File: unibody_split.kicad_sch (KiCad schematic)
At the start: 91 parts

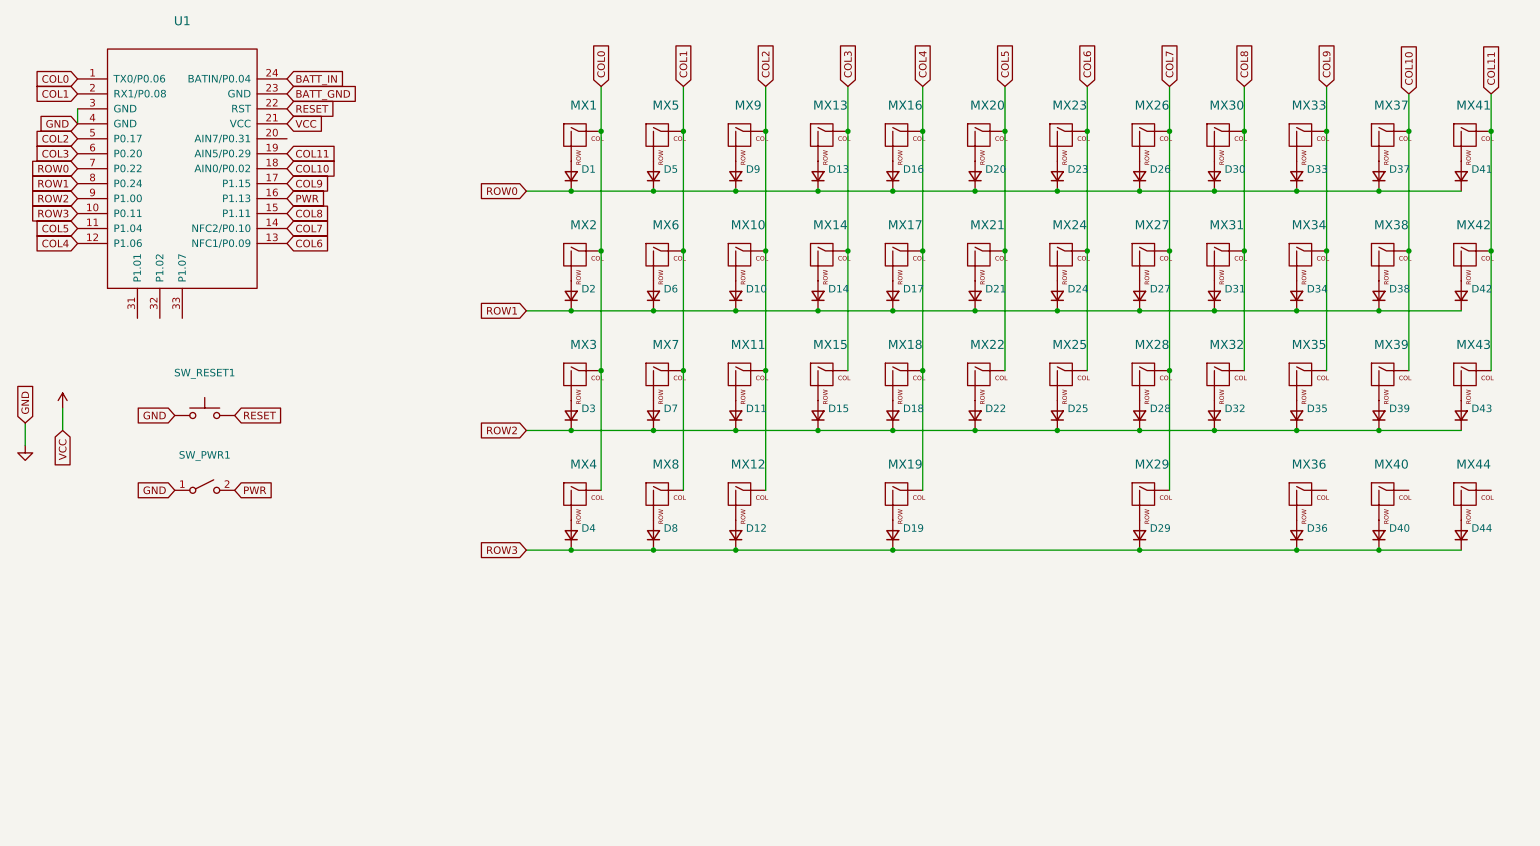
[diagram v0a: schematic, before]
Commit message: Adds kbd library, wires everything up
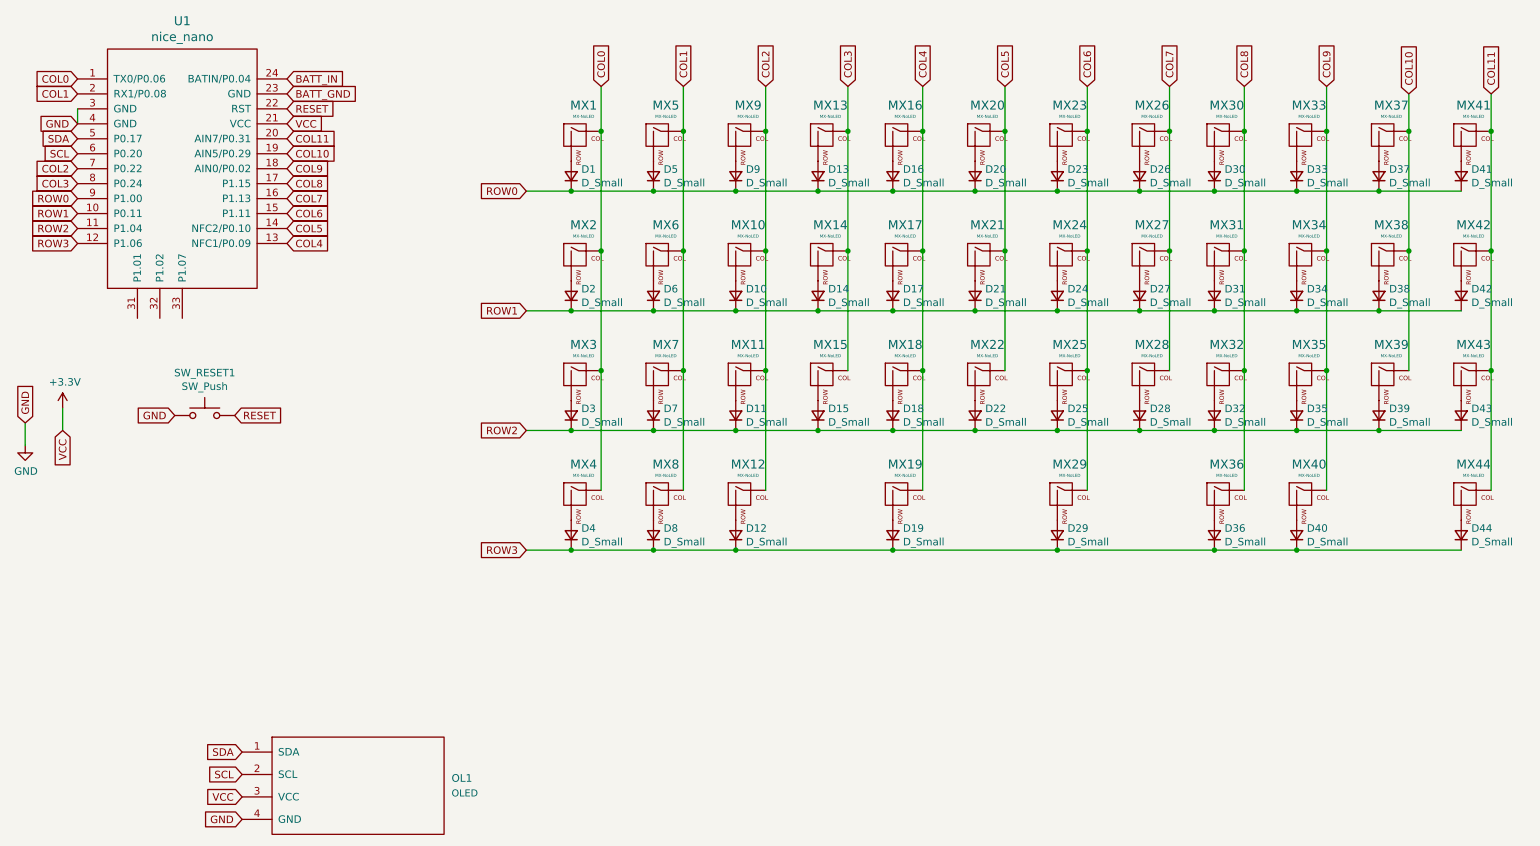
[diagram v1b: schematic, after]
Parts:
- removed SW_PWR1: (no value), symbol Switch:SW_SPST
- added OL1: OLED, kbd:OLED_v2, symbol kbd:OLED
- D1, D10, D11, D12, D13, D14, D15, D16, D17, D18, D19, D2, D20, D21, D22, D23, D24, D25, D26, D27, D28, D29, D3, D30, D31, D32, D33, D34, D35, D36, D37, D38, D39, D4, D40, D41, D42, D43, D44, D5, D6, D7, D8, D9: value (none) -> D_Small; footprint (none) -> Diode_SMD:D_SOD-123
- MX1, MX10, MX11, MX13, MX14, MX15, MX16, MX17, MX18, MX20, MX21, MX22, MX23, MX24, MX25, MX26, MX27, MX28, MX30, MX31, MX32, MX33, MX34, MX35, MX37, MX38, MX39, MX43, MX5, MX6, MX7, MX9: value (none) -> MX-NoLED; footprint (none) -> MX_Only:MXOnly-1U-Hotswap
- MX12, MX19, MX2, MX29, MX3, MX36, MX4, MX40, MX41, MX42, MX44, MX8: value (none) -> MX-NoLED
- SW_RESET1: value (none) -> SW_Push; footprint (none) -> random-keyboard-parts:SKQG-1155865
- U1: value (none) -> nice_nano; footprint (none) -> nice-nano-kicad:nice_nano
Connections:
- net PWR is gone; now on net COL7: U1.16 (P1.13)
- net +3V3: now also OL1.3 (VCC)
- net COL10: now also U1.19 (AIN5/P0.29); no longer U1.18 (AIN0/P0.02)
- net COL11: now also MX44.1 (COL), U1.20 (AIN7/P0.31); no longer U1.19 (AIN5/P0.29)
- net COL2: now also U1.7 (P0.22); no longer U1.5 (P0.17)
- net COL3: now also U1.8 (P0.24); no longer U1.6 (P0.20)
- net COL4: now also U1.13 (NFC1/P0.09); no longer U1.12 (P1.06)
- net COL5: now also U1.14 (NFC2/P0.10); no longer U1.11 (P1.04)
- net COL6: now also MX29.1 (COL), U1.15 (P1.11); no longer U1.13 (NFC1/P0.09)
- net COL7: no longer MX29.1 (COL), U1.14 (NFC2/P0.10)
- net COL8: now also MX36.1 (COL), U1.17 (P1.15); no longer U1.15 (P1.11)
- net COL9: now also MX40.1 (COL), U1.18 (AIN0/P0.02); no longer U1.17 (P1.15)
- net GND: now also OL1.4 (GND)
- net ROW0: now also U1.9 (P1.00); no longer U1.7 (P0.22)
- net ROW1: now also U1.10 (P0.11); no longer U1.8 (P0.24)
- net ROW2: now also U1.11 (P1.04); no longer U1.9 (P1.00)
- net ROW3: now also U1.12 (P1.06); no longer U1.10 (P0.11)
- new net SCL: OL1.2 (SCL), U1.6 (P0.20)
- new net SDA: OL1.1 (SDA), U1.5 (P0.17)
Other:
- moved on the sheet: D29, D36, D40, MX29, MX36, MX40

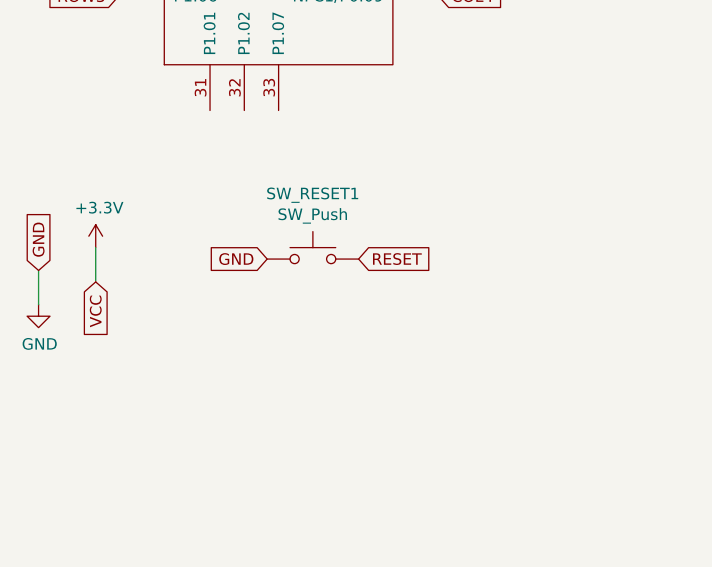
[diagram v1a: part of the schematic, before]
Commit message: Adds smaller reset switch, JST for battery
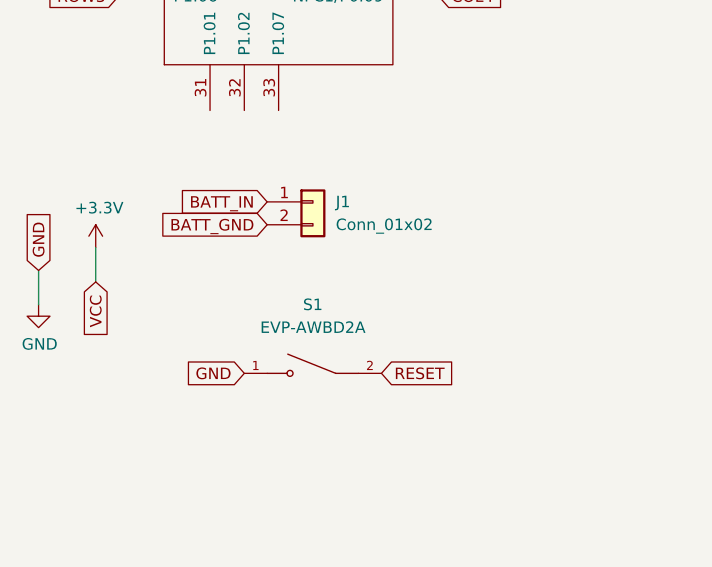
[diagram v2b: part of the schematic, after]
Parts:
- removed SW_RESET1: SW_Push, random-keyboard-parts:SKQG-1155865, symbol Switch:SW_Push
- added J1: Conn_01x02, Connector_JST:JST_PH_S2B-PH-SM4-TB_1x02-1MP_P2.00mm_Horizontal, symbol Connector_Generic:Conn_01x02
- added S1: EVP-AWBD2A, switches:SW_EVP-AWBD2A, symbol EVP-AWBD2A:EVP-AWBD2A
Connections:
- net BATT_GND: now also J1.2 (Pin_2)
- net BATT_IN: now also J1.1 (Pin_1)
- net GND: now also S1.1
- net RESET: now also S1.2
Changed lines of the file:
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@@
     )
   )
-  (global_label "GND" (shape input) (at 43.18 87.63 180) (fields_autoplaced)
+  (global_label "GND" (shape input) (at 40.64 100.33 180) (fields_autoplaced)
     (effects (font (size 1.27 1.27)) (justify right))
-    (property "Intersheet References" "${INTERSHEET_REFS}" (id 0) (at 0 0 0)
+    (property "Intersheet References" "${INTERSHEET_REFS}" (id 0) (at -2.54 12.7 0)
       (effects (font (size 1.27 1.27)) hide)
     )
@@
     (property "Intersheet References" "${INTERSHEET_REFS}" (id 0) (at 0 0 0)
       (effects (font (size 1.27 1.27)) hide)
+    )
+  )
+  (global_label "BATT_IN" (shape input) (at 43.18 81.28 180) (fields_autoplaced)
+    (effects (font (size 1.27 1.27)) (justify right))
+    (property "Intersheet References" "${INTERSHEET_REFS}" (id 0) (at 33.6591 81.2006 0)
+      (effects (font (size 1.27 1.27)) (justify right) hide)
     )
   )
@@
     )
   )
-  (global_label "RESET" (shape input) (at 53.34 87.63 0) (fields_autoplaced)
-    (effects (font (size 1.27 1.27)) (justify left))
-    (property "Intersheet References" "${INTERSHEET_REFS}" (id 0) (at 0 0 0)
+  (global_label "RESET" (shape input) (at 55.88 100.33 0) (fields_autoplaced)
+    (effects (font (size 1.27 1.27)) (justify left))
+    (property "Intersheet References" "${INTERSHEET_REFS}" (id 0) (at 2.54 12.7 0)
       (effects (font (size 1.27 1.27)) hide)
     )
@@
     (property "Intersheet References" "${INTERSHEET_REFS}" (id 0) (at 0 0 0)
       (effects (font (size 1.27 1.27)) hide)
+    )
+  )
+  (global_label "BATT_GND" (shape input) (at 43.18 83.82 180) (fields_autoplaced)
+    (effects (font (size 1.27 1.27)) (justify right))
+    (property "Intersheet References" "${INTERSHEET_REFS}" (id 0) (at 31.7239 83.7406 0)
+      (effects (font (size 1.27 1.27)) (justify right) hide)
     )
   )
@@
     (pin "2")
   )
-  (symbol (lib_id "Switch:SW_Push") (at 48.26 87.63 0) (unit 1)
-    (in_bom yes) (on_board yes)
-    (property "Reference" "SW_RESET1" (id 0) (at 48.26 80.391 0))
-    (property "Value" "SW_Push" (id 1) (at 48.26 82.7024 0))
-    (property "Footprint" "random-keyboard-parts:SKQG-1155865" (id 2) (at 48.26 82.55 0)
-      (effects (font (size 1.27 1.27)) hide)
-    )
-    (property "Datasheet" "~" (id 3) (at 48.26 82.55 0)
+  (symbol (lib_id "EVP-AWBD2A:EVP-AWBD2A") (at 48.26 100.33 0) (unit 1)
+    (in_bom yes) (on_board yes) (fields_autoplaced)
+    (property "Reference" "S1" (id 0) (at 48.26 92.71 0))
+    (property "Value" "EVP-AWBD2A" (id 1) (at 48.26 95.25 0))
+    (property "Footprint" "switches:SW_EVP-AWBD2A" (id 2) (at 48.26 100.33 0)
+      (effects (font (size 1.27 1.27)) (justify left bottom) hide)
+    )
+    (property "Datasheet" "" (id 3) (at 48.26 100.33 0)
+      (effects (font (size 1.27 1.27)) (justify left bottom) hide)
+    )
+    (property "DESCRIPTION" "Tactile Switch SPST-NO Top Actuated Surface Mount" (id 4) (at 48.26 100.33 0)
+      (effects (font (size 1.27 1.27)) (justify left bottom) hide)
+    )
+    (property "AVAILABILITY" "Bad" (id 5) (at 48.26 100.33 0)
+      (effects (font (size 1.27 1.27)) (justify left bottom) hide)
+    )
+    (property "PRICE" "None" (id 6) (at 48.26 100.33 0)
+      (effects (font (size 1.27 1.27)) (justify left bottom) hide)
+    )
+    (property "MF" "Panasonic" (id 7) (at 48.26 100.33 0)
+      (effects (font (size 1.27 1.27)) (justify left bottom) hide)
+    )
+    (property "PACKAGE" "None" (id 8) (at 48.26 100.33 0)
+      (effects (font (size 1.27 1.27)) (justify left bottom) hide)
+    )
+    (property "MP" "EVP-AWBD2A" (id 9) (at 48.26 100.33 0)
+      (effects (font (size 1.27 1.27)) (justify left bottom) hide)
+    )
+    (pin "1")
+    (pin "2")
+  )
+  (symbol (lib_id "Connector_Generic:Conn_01x02") (at 48.26 81.28 0) (unit 1)
+    (in_bom yes) (on_board yes) (fields_autoplaced)
+    (property "Reference" "J1" (id 0) (at 50.8 81.2799 0)
+      (effects (font (size 1.27 1.27)) (justify left))
+    )
+    (property "Value" "Conn_01x02" (id 1) (at 50.8 83.8199 0)
+      (effects (font (size 1.27 1.27)) (justify left))
+    )
+    (property "Footprint" "Connector_JST:JST_PH_S2B-PH-SM4-TB_1x02-1MP_P2.00mm_Horizontal" (id 2) (at 48.26 81.28 0)
+      (effects (font (size 1.27 1.27)) hide)
+    )
+    (property "Datasheet" "~" (id 3) (at 48.26 81.28 0)
       (effects (font (size 1.27 1.27)) hide)
     )
@@
       (reference "D44") (unit 1) (value "D_Small") (footprint "Diode_SMD:D_SOD-123")
     )
+    (path "/79982c91-be75-4df7-b1d6-4ba9b6327eb9"
+      (reference "J1") (unit 1) (value "Conn_01x02") (footprint "Connector_JST:JST_PH_S2B-PH-SM4-TB_1x02-1MP_P2.00mm_Horizontal")
+    )
     (path "/00000000-0000-0000-0000-000062858741"
       (reference "MX1") (unit 1) (value "MX-NoLED") (footprint "MX_Only:MXOnly-1U-Hotswap")
@@
       (reference "OL1") (unit 1) (value "OLED") (footprint "kbd:OLED_v2")
     )
-    (path "/00000000-0000-0000-0000-000062927c00"
-      (reference "SW_RESET1") (unit 1) (value "SW_Push") (footprint "random-keyboard-parts:SKQG-1155865")
+    (path "/0b819230-8318-4e3a-9e01-b696526ebe96"
+      (reference "S1") (unit 1) (value "EVP-AWBD2A") (footprint "switches:SW_EVP-AWBD2A")
     )
     (path "/00000000-0000-0000-0000-00006284d38e"

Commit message: Update JST header to XH
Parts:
- J1: footprint Connector_JST:JST_PH_S2B-PH-SM4-TB_1x02-1MP_P2.00mm_Horizontal -> Connector_JST:JST_XH_S2B-XH-A_1x02_P2.50mm_Horizontal
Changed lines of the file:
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@@
       (effects (font (size 1.27 1.27)) (justify left))
     )
-    (property "Footprint" "Connector_JST:JST_PH_S2B-PH-SM4-TB_1x02-1MP_P2.00mm_Horizontal" (id 2) (at 48.26 81.28 0)
+    (property "Footprint" "Connector_JST:JST_XH_S2B-XH-A_1x02_P2.50mm_Horizontal" (id 2) (at 48.26 81.28 0)
       (effects (font (size 1.27 1.27)) hide)
     )
@@
     )
     (path "/79982c91-be75-4df7-b1d6-4ba9b6327eb9"
-      (reference "J1") (unit 1) (value "Conn_01x02") (footprint "Connector_JST:JST_PH_S2B-PH-SM4-TB_1x02-1MP_P2.00mm_Horizontal")
+      (reference "J1") (unit 1) (value "Conn_01x02") (footprint "Connector_JST:JST_XH_S2B-XH-A_1x02_P2.50mm_Horizontal")
     )
     (path "/00000000-0000-0000-0000-000062858741"

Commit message: Use sma diodes
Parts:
- D1, D10, D11, D12, D13, D14, D15, D16, D17, D18, D19, D2, D20, D21, D22, D23, D24, D25, D26, D27, D28, D29, D3, D30, D31, D32, D33, D34, D35, D36, D37, D38, D39, D4, D40, D41, D42, D43, D44, D5, D6, D7, D8, D9: footprint Diode_SMD:D_SOD-123 -> Diode_SMD:D_SMA_Handsoldering

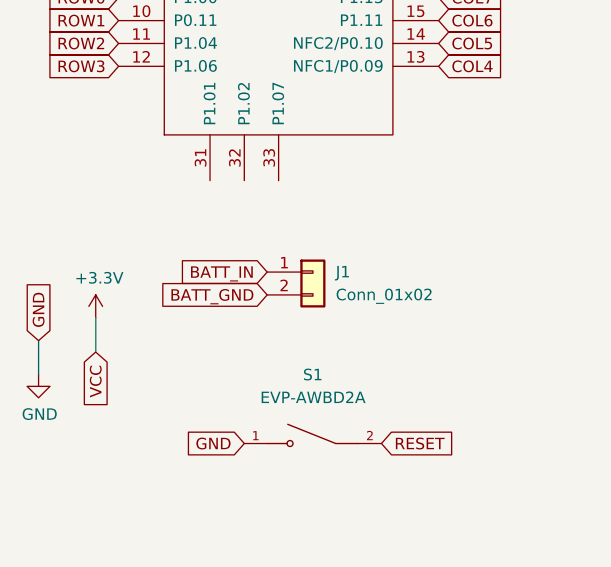
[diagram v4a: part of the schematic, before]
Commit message: Uses JST smd
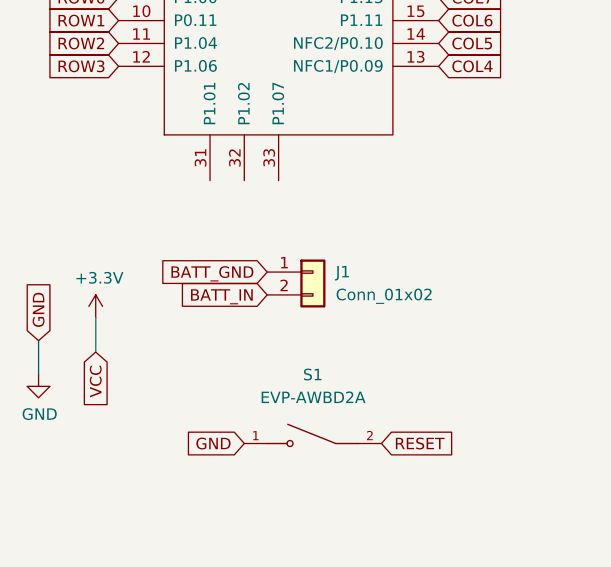
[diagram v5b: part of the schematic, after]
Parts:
- J1: footprint Connector_JST:JST_XH_S2B-XH-A_1x02_P2.50mm_Horizontal -> Connectors:JST-2-SMD
- MX29: footprint MX_Only:MXOnly-2U-Hotswap -> MX_Only:MXOnly-1U-Hotswap
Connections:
- net BATT_GND: now also J1.1 (Pin_1); no longer J1.2 (Pin_2)
- net BATT_IN: now also J1.2 (Pin_2); no longer J1.1 (Pin_1)
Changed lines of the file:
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@@
     )
   )
-  (global_label "BATT_IN" (shape input) (at 43.18 81.28 180) (fields_autoplaced)
+  (global_label "BATT_IN" (shape input) (at 43.18 83.82 180) (fields_autoplaced)
     (effects (font (size 1.27 1.27)) (justify right))
-    (property "Intersheet References" "${INTERSHEET_REFS}" (id 0) (at 33.6591 81.2006 0)
+    (property "Intersheet References" "${INTERSHEET_REFS}" (id 0) (at 33.6591 83.7406 0)
       (effects (font (size 1.27 1.27)) (justify right) hide)
     )
@@
     )
   )
-  (global_label "BATT_GND" (shape input) (at 43.18 83.82 180) (fields_autoplaced)
+  (global_label "BATT_GND" (shape input) (at 43.18 81.28 180) (fields_autoplaced)
     (effects (font (size 1.27 1.27)) (justify right))
-    (property "Intersheet References" "${INTERSHEET_REFS}" (id 0) (at 31.7239 83.7406 0)
+    (property "Intersheet References" "${INTERSHEET_REFS}" (id 0) (at 31.7239 81.2006 0)
       (effects (font (size 1.27 1.27)) (justify right) hide)
     )
@@
       (effects (font (size 0.508 0.508)))
     )
-    (property "Footprint" "MX_Only:MXOnly-2U-Hotswap" (id 2) (at 178.435 102.235 0)
+    (property "Footprint" "MX_Only:MXOnly-1U-Hotswap" (id 2) (at 178.435 102.235 0)
       (effects (font (size 1.524 1.524)) hide)
     )
@@
       (effects (font (size 1.27 1.27)) (justify left))
     )
-    (property "Footprint" "Connector_JST:JST_XH_S2B-XH-A_1x02_P2.50mm_Horizontal" (id 2) (at 48.26 81.28 0)
+    (property "Footprint" "Connectors:JST-2-SMD" (id 2) (at 48.26 81.28 0)
       (effects (font (size 1.27 1.27)) hide)
     )
@@
     )
     (path "/79982c91-be75-4df7-b1d6-4ba9b6327eb9"
-      (reference "J1") (unit 1) (value "Conn_01x02") (footprint "Connector_JST:JST_XH_S2B-XH-A_1x02_P2.50mm_Horizontal")
+      (reference "J1") (unit 1) (value "Conn_01x02") (footprint "Connectors:JST-2-SMD")
     )
     (path "/00000000-0000-0000-0000-000062858741"
@@
     )
     (path "/00000000-0000-0000-0000-0000628a8e1b"
-      (reference "MX29") (unit 1) (value "MX-NoLED") (footprint "MX_Only:MXOnly-2U-Hotswap")
+      (reference "MX29") (unit 1) (value "MX-NoLED") (footprint "MX_Only:MXOnly-1U-Hotswap")
     )
     (path "/00000000-0000-0000-0000-00006286915c"

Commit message: Move nice nano to new board edge, zone fills
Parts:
- S1: footprint switches:SW_EVP-AWBD2A -> random-keyboard-parts:SKQG-1155865
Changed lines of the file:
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@@
     (property "Reference" "S1" (id 0) (at 48.26 92.71 0))
     (property "Value" "EVP-AWBD2A" (id 1) (at 48.26 95.25 0))
-    (property "Footprint" "switches:SW_EVP-AWBD2A" (id 2) (at 48.26 100.33 0)
+    (property "Footprint" "random-keyboard-parts:SKQG-1155865" (id 2) (at 48.26 100.33 0)
       (effects (font (size 1.27 1.27)) (justify left bottom) hide)
     )
@@
     )
     (path "/0b819230-8318-4e3a-9e01-b696526ebe96"
-      (reference "S1") (unit 1) (value "EVP-AWBD2A") (footprint "switches:SW_EVP-AWBD2A")
+      (reference "S1") (unit 1) (value "EVP-AWBD2A") (footprint "random-keyboard-parts:SKQG-1155865")
     )
     (path "/00000000-0000-0000-0000-00006284d38e"

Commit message: Fixes M29 using wrong footprint
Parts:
- MX29: footprint MX_Only:MXOnly-1U-Hotswap -> MX_Only:MXOnly-2U-Hotswap
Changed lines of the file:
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@@
       (effects (font (size 0.508 0.508)))
     )
-    (property "Footprint" "MX_Only:MXOnly-1U-Hotswap" (id 2) (at 178.435 102.235 0)
+    (property "Footprint" "MX_Only:MXOnly-2U-Hotswap" (id 2) (at 178.435 102.235 0)
       (effects (font (size 1.524 1.524)) hide)
     )
@@
     )
     (path "/00000000-0000-0000-0000-0000628a8e1b"
-      (reference "MX29") (unit 1) (value "MX-NoLED") (footprint "MX_Only:MXOnly-1U-Hotswap")
+      (reference "MX29") (unit 1) (value "MX-NoLED") (footprint "MX_Only:MXOnly-2U-Hotswap")
     )
     (path "/00000000-0000-0000-0000-00006286915c"
